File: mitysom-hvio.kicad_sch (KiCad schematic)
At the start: 20 parts, among them J1 Plug_Samtec_SEAM-50-02.0-L-08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, U1 TXS0102DQER, U2 LSF0108RKSR, U3 LSF0108RKSR

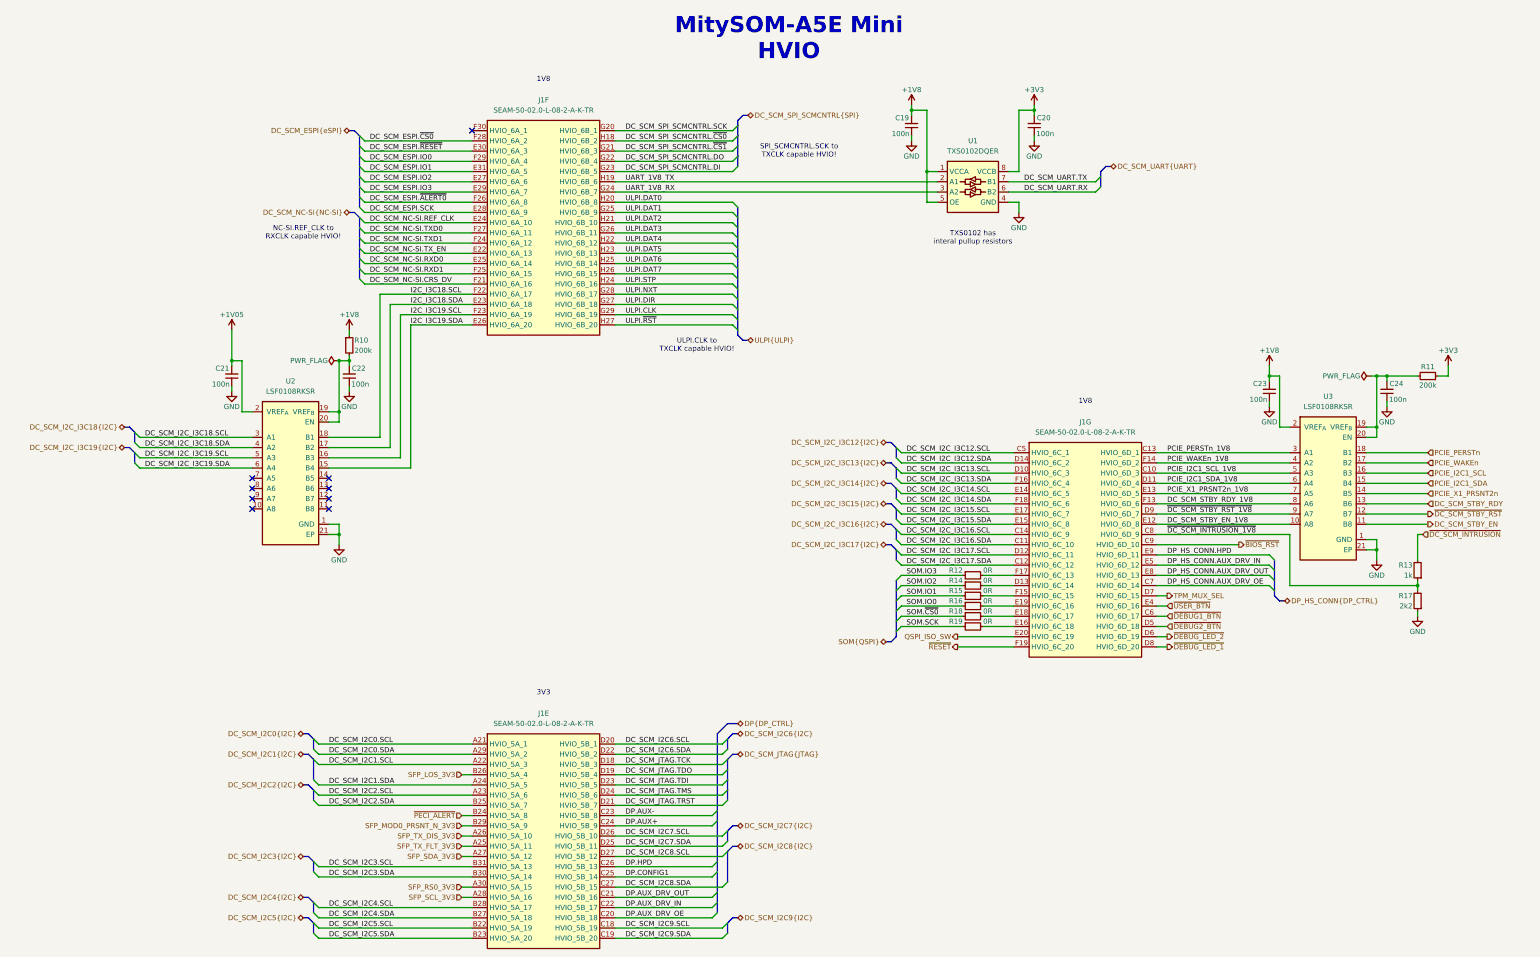
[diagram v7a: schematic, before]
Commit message: [#100595] Update connections according to client request
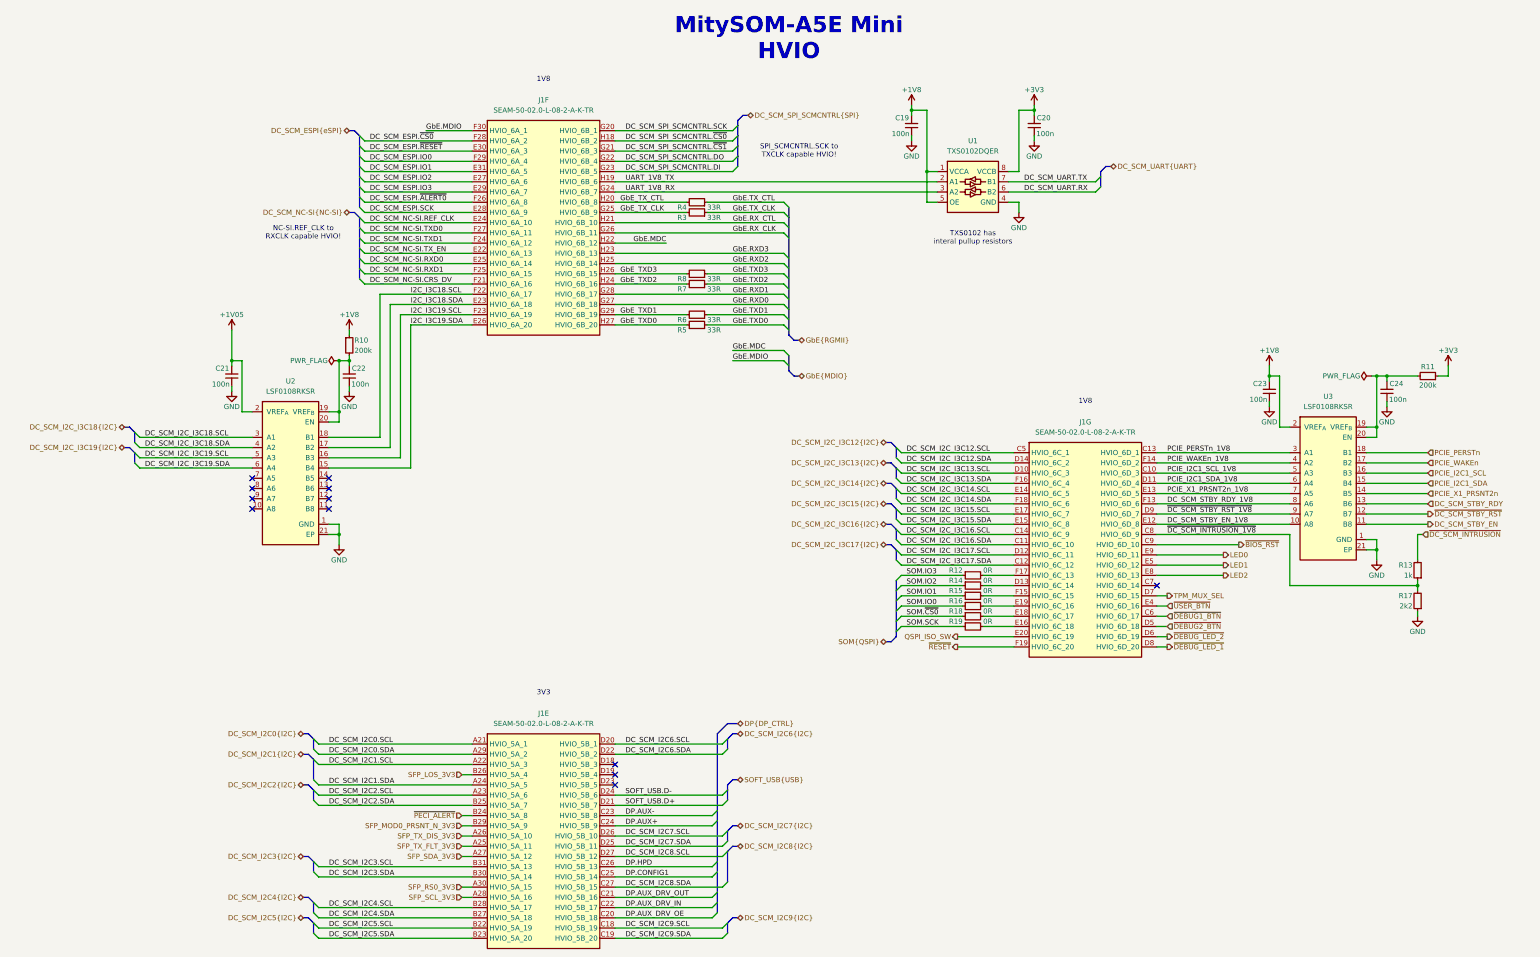
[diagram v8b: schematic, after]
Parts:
- added R3, R4, R5, R6, R7, R8: R_33R_0402, antmicro-footprints:R_0402_1005Metric, symbol antmicroResistors0402:R_33R_0402
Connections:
- net GbE.MDIO: now reaches J1.F30 (HVIO_6A_1)
- net DC_SCM_JTAG.TCK: no longer names the net of J1.D18 (HVIO_5B_3)
- net DC_SCM_JTAG.TDI: no longer names the net of J1.D23 (HVIO_5B_5)
- net DC_SCM_JTAG.TDO: no longer names the net of J1.D19 (HVIO_5B_4)
- net DC_SCM_JTAG.TMS renamed SOFT_USB.D-
- net DC_SCM_JTAG.TRST renamed SOFT_USB.D+
- net DP_HS_CONN.AUX_DRV_IN renamed LED1
- net DP_HS_CONN.AUX_DRV_OE: no longer names the net of J1.C7 (HVIO_6D_14)
- net DP_HS_CONN.AUX_DRV_OUT renamed LED2
- net DP_HS_CONN.HPD renamed LED0
- net ULPI.CLK renamed GbE_TXD1
- net GbE_TXD1: now also R6.2
- net ULPI.DAT0 renamed GbE_TX_CTL
- net GbE_TX_CTL: now also R4.2
- net ULPI.DAT1 renamed GbE_TX_CLK
- net GbE_TX_CLK: now also R3.2
- net ULPI.DAT2 renamed GbE.RX_CTL
- net ULPI.DAT3 renamed GbE.RX_CLK
- net ULPI.DAT4 renamed GbE.MDC
- net ULPI.DAT5 renamed GbE.RXD3
- net ULPI.DAT6 renamed GbE.RXD2
- net ULPI.DAT7 renamed GbE_TXD3
- net GbE_TXD3: now also R8.2
- net ULPI.DIR renamed GbE.RXD0
- net ULPI.NXT renamed GbE.RXD1
- net ULPI.STP renamed GbE_TXD2
- net GbE_TXD2: now also R7.2
- net ULPI.~{RST} renamed GbE_TXD0
- net GbE_TXD0: now also R5.2
- new net GbE.TXD0: R5.1
- new net GbE.TXD1: R6.1
- new net GbE.TXD2: R7.1
- new net GbE.TXD3: R8.1
- new net GbE.TX_CLK: R3.1
- new net GbE.TX_CTL: R4.1
- no-connect marks 9 -> 12
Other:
- note removed: "ULPI.CLK to TXCLK capable HVIO!"
